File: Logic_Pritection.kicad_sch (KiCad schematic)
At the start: 11 parts

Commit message: Одна стойка
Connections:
- net +5VD: now also D7.5 (Vcc)
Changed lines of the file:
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@@
     (pin "1")
   )
-  (symbol (lib_id "power:+5VD") (at 135.255 79.502 0) (unit 1)
+  (symbol (lib_id "power:+5VD") (at 135.382 79.502 0) (unit 1)
     (in_bom yes) (on_board yes)
-    (property "Reference" "#PWR018" (id 0) (at 135.255 83.312 0)
+    (property "Reference" "#PWR018" (id 0) (at 135.382 83.312 0)
       (effects (font (size 1.27 1.27)) hide)
     )
-    (property "Value" "+5VD" (id 1) (at 138.557 78.74 0))
-    (property "Footprint" "" (id 2) (at 135.255 79.502 0)
+    (property "Value" "+5VD" (id 1) (at 138.684 78.74 0))
+    (property "Footprint" "" (id 2) (at 135.382 79.502 0)
       (effects (font (size 1.27 1.27)) hide)
     )
-    (property "Datasheet" "" (id 3) (at 135.255 79.502 0)
+    (property "Datasheet" "" (id 3) (at 135.382 79.502 0)
       (effects (font (size 1.27 1.27)) hide)
     )

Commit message: Первая сырая расстановка, неполная
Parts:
- added R125, R127: 2k, Resistor_SMD:R_0805_2012Metric_Pad1.20x1.40mm_HandSolder, symbol Device:R_Small
- added R126, R128: 1k, Resistor_SMD:R_0805_2012Metric_Pad1.20x1.40mm_HandSolder, symbol Device:R_Small
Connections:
- net GND3 renamed GND
- net GND: now also R126.2, R128.2
- net PWM_Input_H1: no longer names the net of D7.1 (A), R13.2, R15.1
- net PWM_Input_H1: now also R125.2, R126.1
- net PWM_Input_L1: no longer names the net of D7.2 (B), R14.2, R16.1
- net PWM_Input_L1: now also R127.2, R128.1
- new net HB1_BOT: R127.1
- new net HB1_TOP: R125.1

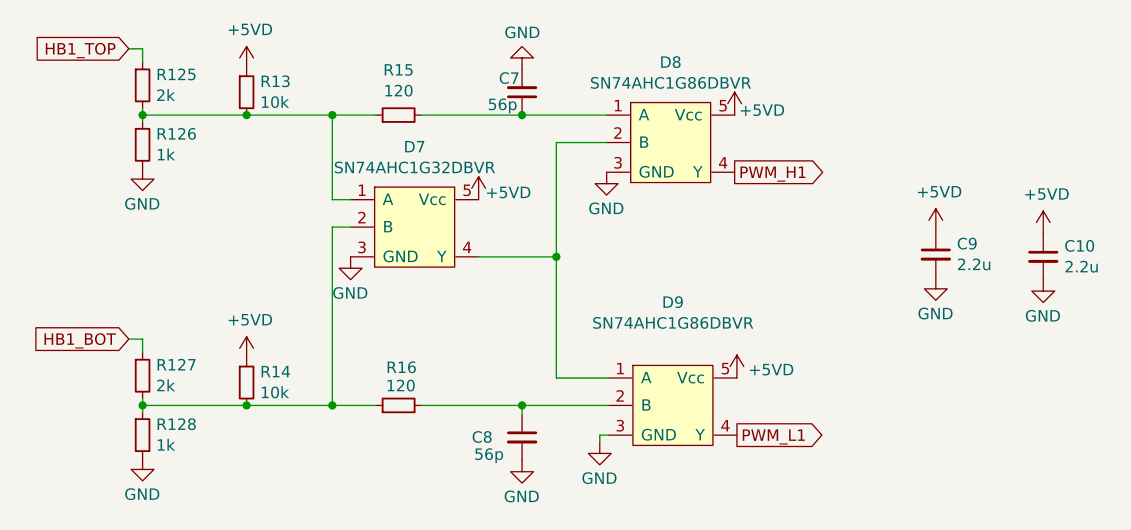
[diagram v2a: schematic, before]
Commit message: Всё влезло, осталься компаратор на NTC
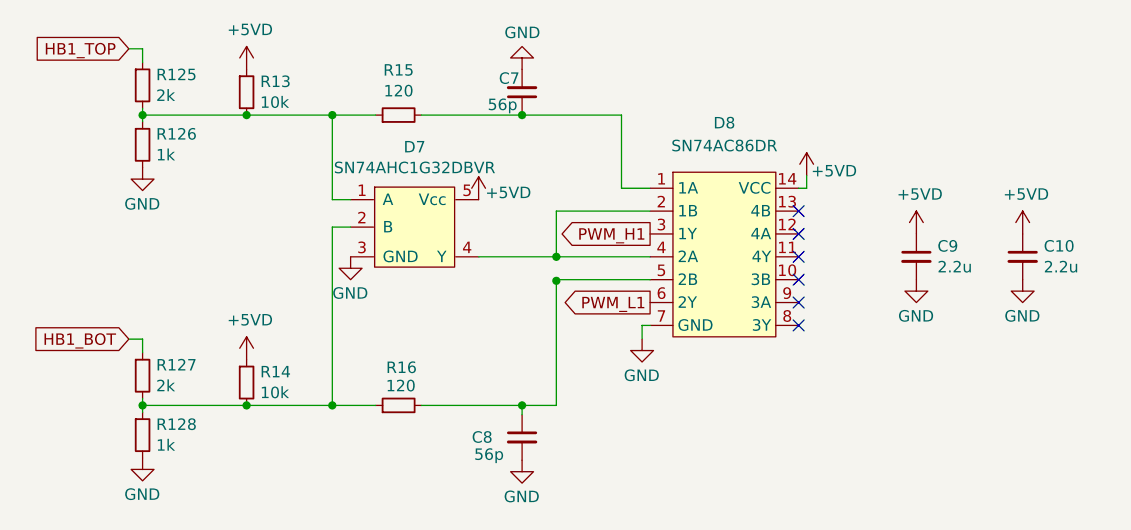
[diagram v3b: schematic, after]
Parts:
- removed D8, D9: SN74AHC1G86DBVR, Package_TO_SOT_SMD:SOT-23-5_HandSoldering, symbol Logic:SN74AHC1G86DBVR
- added D8: SN74AC86DR, Package_SO:SOIC-14_3.9x8.7mm_P1.27mm, symbol Logic_My:SN74AC86DR
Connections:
- net +5VD: now also D8.14 (VCC)
- net GND: now also D8.7 (GND)
- net PWM_H1: now also D8.3 (1Y)
- net PWM_L1: now also D8.6 (2Y)
- net at C8.1, R16.2: now also D8.5 (2B)
- net at D7.4 (Y): now also D8.2 (1B), D8.4 (2A)
- net at C7.1, R15.2: now also D8.1 (1A)
- no-connect marks 0 -> 6
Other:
- moved on the sheet: C10, C9

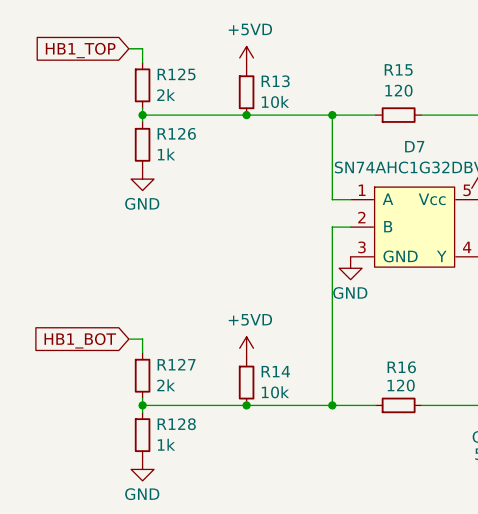
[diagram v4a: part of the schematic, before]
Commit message: Исправил ошибки, добавил резисторы в затвор, ревизия 2.0
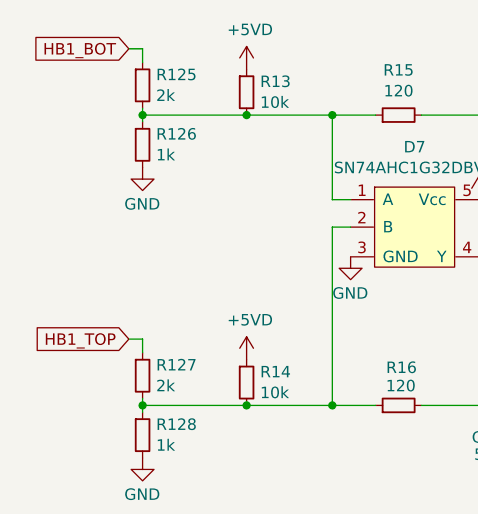
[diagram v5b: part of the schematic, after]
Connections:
- net HB1_BOT: now also R125.1; no longer R127.1
- net HB1_TOP: now also R127.1; no longer R125.1
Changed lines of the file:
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@@
     )
   )
-  (global_label "HB1_BOT" (shape input) (at 96.52 94.996 180) (fields_autoplaced)
+  (global_label "HB1_BOT" (shape input) (at 96.52 62.738 180) (fields_autoplaced)
     (effects (font (size 1.27 1.27)) (justify right))
-    (property "Intersheet References" "${INTERSHEET_REFS}" (id 0) (at 85.7612 94.9166 0)
+    (property "Intersheet References" "${INTERSHEET_REFS}" (id 0) (at 85.7612 62.6586 0)
       (effects (font (size 1.27 1.27)) (justify right) hide)
     )
@@
     )
   )
-  (global_label "HB1_TOP" (shape input) (at 96.52 62.738 180) (fields_autoplaced)
+  (global_label "HB1_TOP" (shape input) (at 96.52 94.996 180) (fields_autoplaced)
     (effects (font (size 1.27 1.27)) (justify right))
-    (property "Intersheet References" "${INTERSHEET_REFS}" (id 0) (at 85.7612 62.6586 0)
+    (property "Intersheet References" "${INTERSHEET_REFS}" (id 0) (at 85.7612 94.9166 0)
       (effects (font (size 1.27 1.27)) (justify right) hide)
     )

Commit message: Версия для резонита REV2.1
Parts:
- removed C7, C8: 56p, Capacitor_SMD:C_0805_2012Metric_Pad1.18x1.45mm_HandSolder, symbol Device:C_Small
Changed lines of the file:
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@@
   (junction (at 119.126 102.362) (diameter 0) (color 0 0 0 0)
   )
-  (junction (at 140.208 102.362) (diameter 0) (color 0 0 0 0)
-  )
   (junction (at 144.018 85.852) (diameter 0) (color 0 0 0 0)
   )
@@
   )
   (junction (at 109.601 70.104) (diameter 0) (color 0 0 0 0)
-  )
-  (junction (at 140.208 70.104) (diameter 0) (color 0 0 0 0)
   )
   (junction (at 98.044 102.362) (diameter 0) (color 0 0 0 0)
@@
     (stroke (width 0) (type default) (color 0 0 0 0))
   )
-  (wire (pts (xy 144.018 102.362) (xy 140.208 102.362))
-    (stroke (width 0) (type default) (color 0 0 0 0))
-  )
   (wire (pts (xy 98.044 101.6) (xy 98.044 102.362))
     (stroke (width 0) (type default) (color 0 0 0 0))
@@
     (stroke (width 0) (type default) (color 0 0 0 0))
   )
-  (wire (pts (xy 140.208 70.104) (xy 151.257 70.104))
+  (wire (pts (xy 129.032 70.104) (xy 151.257 70.104))
     (stroke (width 0) (type default) (color 0 0 0 0))
   )
@@
     (stroke (width 0) (type default) (color 0 0 0 0))
   )
-  (wire (pts (xy 129.032 102.362) (xy 140.208 102.362))
+  (wire (pts (xy 129.032 102.362) (xy 144.018 102.362))
     (stroke (width 0) (type default) (color 0 0 0 0))
   )
@@
     (stroke (width 0) (type default) (color 0 0 0 0))
   )
-  (wire (pts (xy 140.208 102.362) (xy 140.208 103.378))
-    (stroke (width 0) (type default) (color 0 0 0 0))
-  )
   (wire (pts (xy 119.126 82.55) (xy 119.126 102.362))
-    (stroke (width 0) (type default) (color 0 0 0 0))
-  )
-  (wire (pts (xy 129.032 70.104) (xy 140.208 70.104))
     (stroke (width 0) (type default) (color 0 0 0 0))
   )
@@
     (pin "1")
   )
-  (symbol (lib_id "Device:C_Small") (at 140.208 105.918 0) (unit 1)
-    (in_bom yes) (on_board yes)
-    (property "Reference" "C8" (id 0) (at 134.62 105.918 0)
-      (effects (font (size 1.27 1.27)) (justify left))
-    )
-    (property "Value" "56p" (id 1) (at 134.874 107.823 0)
-      (effects (font (size 1.27 1.27)) (justify left))
-    )
-    (property "Footprint" "Capacitor_SMD:C_0805_2012Metric_Pad1.18x1.45mm_HandSolder" (id 2) (at 140.208 105.918 0)
-      (effects (font (size 1.27 1.27)) hide)
-    )
-    (property "Datasheet" "~" (id 3) (at 140.208 105.918 0)
-      (effects (font (size 1.27 1.27)) hide)
-    )
-    (pin "1")
-    (pin "2")
-  )
   (symbol (lib_id "power:GND") (at 98.044 108.204 0) (unit 1)
     (in_bom yes) (on_board yes)
@@
     )
     (property "Datasheet" "" (id 3) (at 98.044 75.946 0)
-      (effects (font (size 1.27 1.27)) hide)
-    )
-    (pin "1")
-  )
-  (symbol (lib_id "power:GND") (at 140.208 108.458 0) (unit 1)
-    (in_bom yes) (on_board yes)
-    (property "Reference" "#PWR0119" (id 0) (at 140.208 114.808 0)
-      (effects (font (size 1.27 1.27)) hide)
-    )
-    (property "Value" "GND" (id 1) (at 138.176 112.522 0)
-      (effects (font (size 1.27 1.27)) (justify left))
-    )
-    (property "Footprint" "" (id 2) (at 140.208 108.458 0)
-      (effects (font (size 1.27 1.27)) hide)
-    )
-    (property "Datasheet" "" (id 3) (at 140.208 108.458 0)
       (effects (font (size 1.27 1.27)) hide)
     )
@@
     (pin "1")
   )
-  (symbol (lib_id "Device:C_Small") (at 140.208 67.564 180) (unit 1)
-    (in_bom yes) (on_board yes)
-    (property "Reference" "C7" (id 0) (at 139.954 66.04 0)
-      (effects (font (size 1.27 1.27)) (justify left))
-    )
-    (property "Value" "56p" (id 1) (at 139.7 68.961 0)
-      (effects (font (size 1.27 1.27)) (justify left))
-    )
-    (property "Footprint" "Capacitor_SMD:C_0805_2012Metric_Pad1.18x1.45mm_HandSolder" (id 2) (at 140.208 67.564 0)
-      (effects (font (size 1.27 1.27)) hide)
-    )
-    (property "Datasheet" "~" (id 3) (at 140.208 67.564 0)
-      (effects (font (size 1.27 1.27)) hide)
-    )
-    (pin "1")
-    (pin "2")
-  )
   (symbol (lib_id "Device:R_Small") (at 126.492 102.362 90) (unit 1)
     (in_bom yes) (on_board yes)
@@
     (pin "5")
   )
-  (symbol (lib_id "power:GND") (at 140.208 65.024 180) (unit 1)
-    (in_bom yes) (on_board yes)
-    (property "Reference" "#PWR0116" (id 0) (at 140.208 58.674 0)
-      (effects (font (size 1.27 1.27)) hide)
-    )
-    (property "Value" "GND" (id 1) (at 142.24 60.96 0)
-      (effects (font (size 1.27 1.27)) (justify left))
-    )
-    (property "Footprint" "" (id 2) (at 140.208 65.024 0)
-      (effects (font (size 1.27 1.27)) hide)
-    )
-    (property "Datasheet" "" (id 3) (at 140.208 65.024 0)
-      (effects (font (size 1.27 1.27)) hide)
-    )
-    (pin "1")
-  )
   (symbol (lib_id "Device:C_Small") (at 195.834 85.852 0) (unit 1)
